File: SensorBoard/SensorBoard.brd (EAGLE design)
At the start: 160 x 100 mm, 44 parts, among them IC1 7805, J1 DCJ0202, U1 MPU-6000QFN-24, X3 MINI-USB-SCHIELD-32005-201

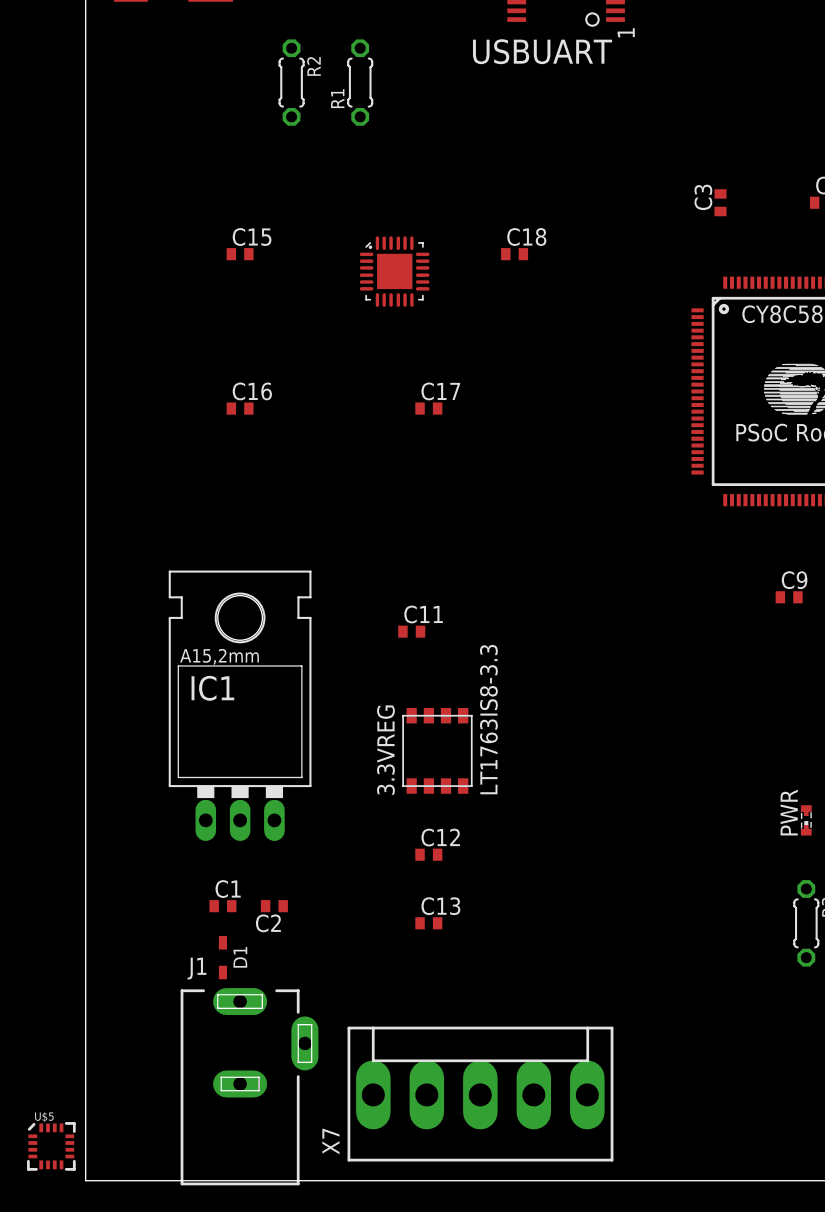
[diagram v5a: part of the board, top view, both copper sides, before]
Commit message: added magnetometer
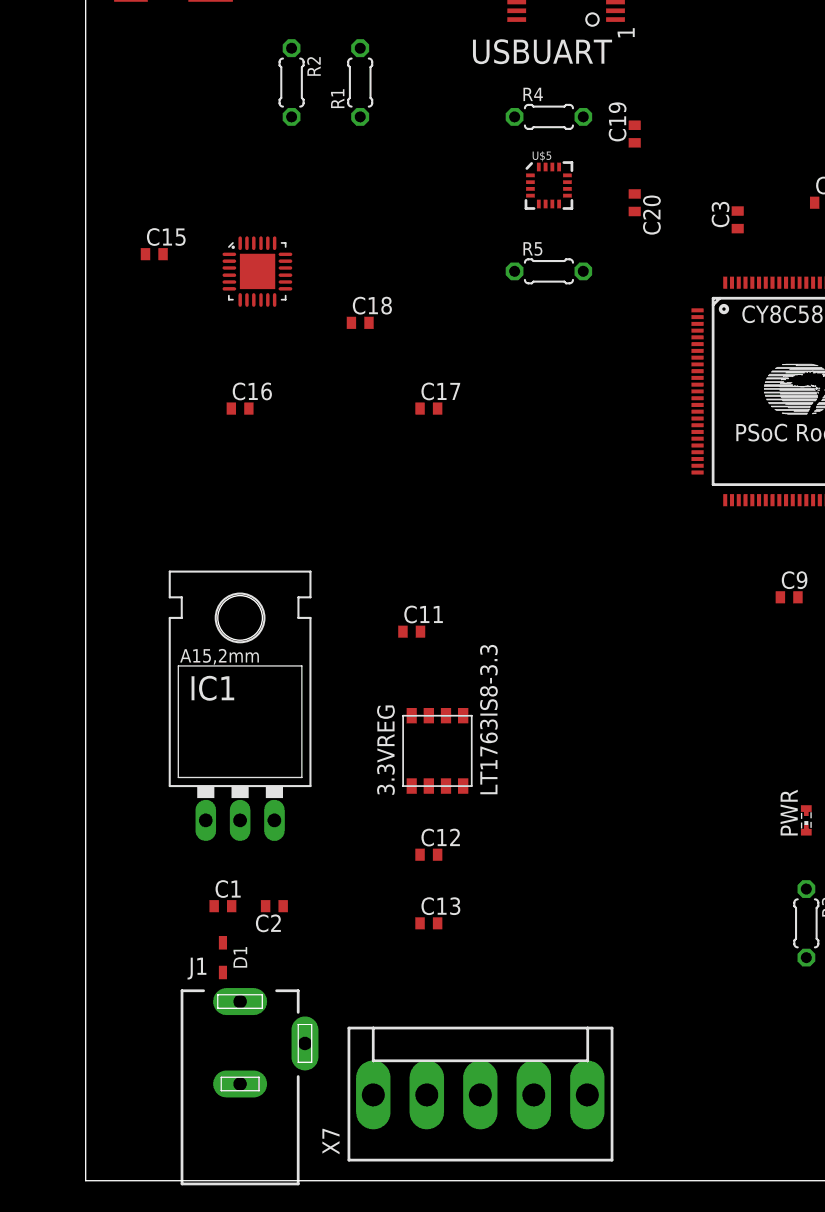
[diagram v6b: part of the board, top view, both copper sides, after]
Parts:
- added C19: .22uF, rcl:C0402
- added C20: 4.7uF, rcl:C0402
- added R4, R5: 4k, resistor:0204/5
- moved U$5 80.1 mm to (34.3, 73.7)
- moved C18 12.5 mm to (20.3, 63.5)
- moved U1 10.2 mm to (12.7, 67.3)
- moved C15 6.35 mm to (5.08, 68.6)
- moved C3 1.80 mm to (48.3, 71.1)
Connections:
- new net N$11: C19.2, U$5.12
- new net N$15: C19.1, U$5.8
- new net N$16: C20.1, U$5.10
- net +3.3V: now also R4.2, R5.2, U$5.13, U$5.2, U$5.4
- net AUXCL1: now also R4.1, U$5.1
- net AUXDA1: now also R5.1, U$5.16
- net GND: now also C20.2, U$5.11, U$5.9

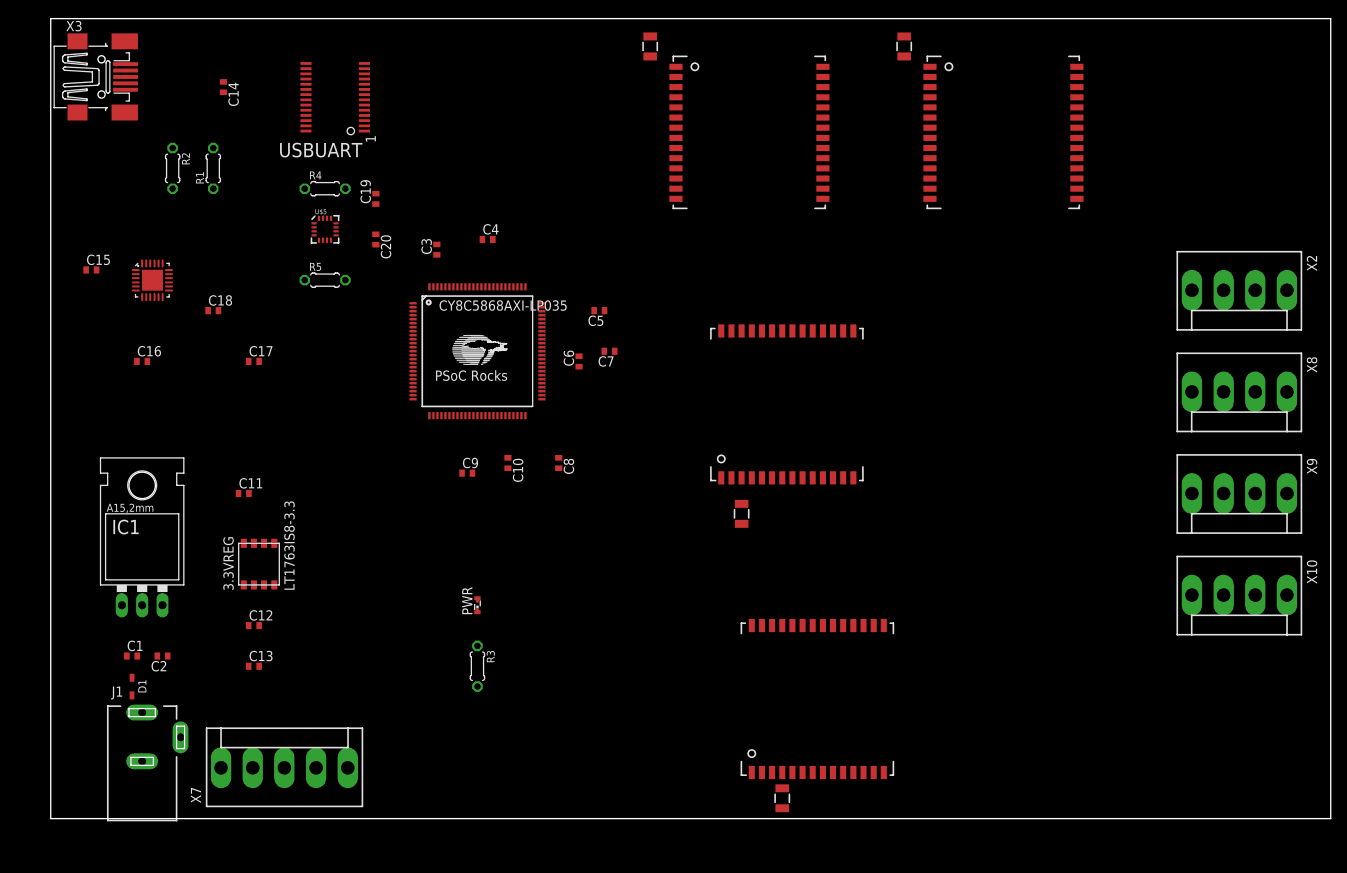
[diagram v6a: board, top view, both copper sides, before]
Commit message: added general pin io
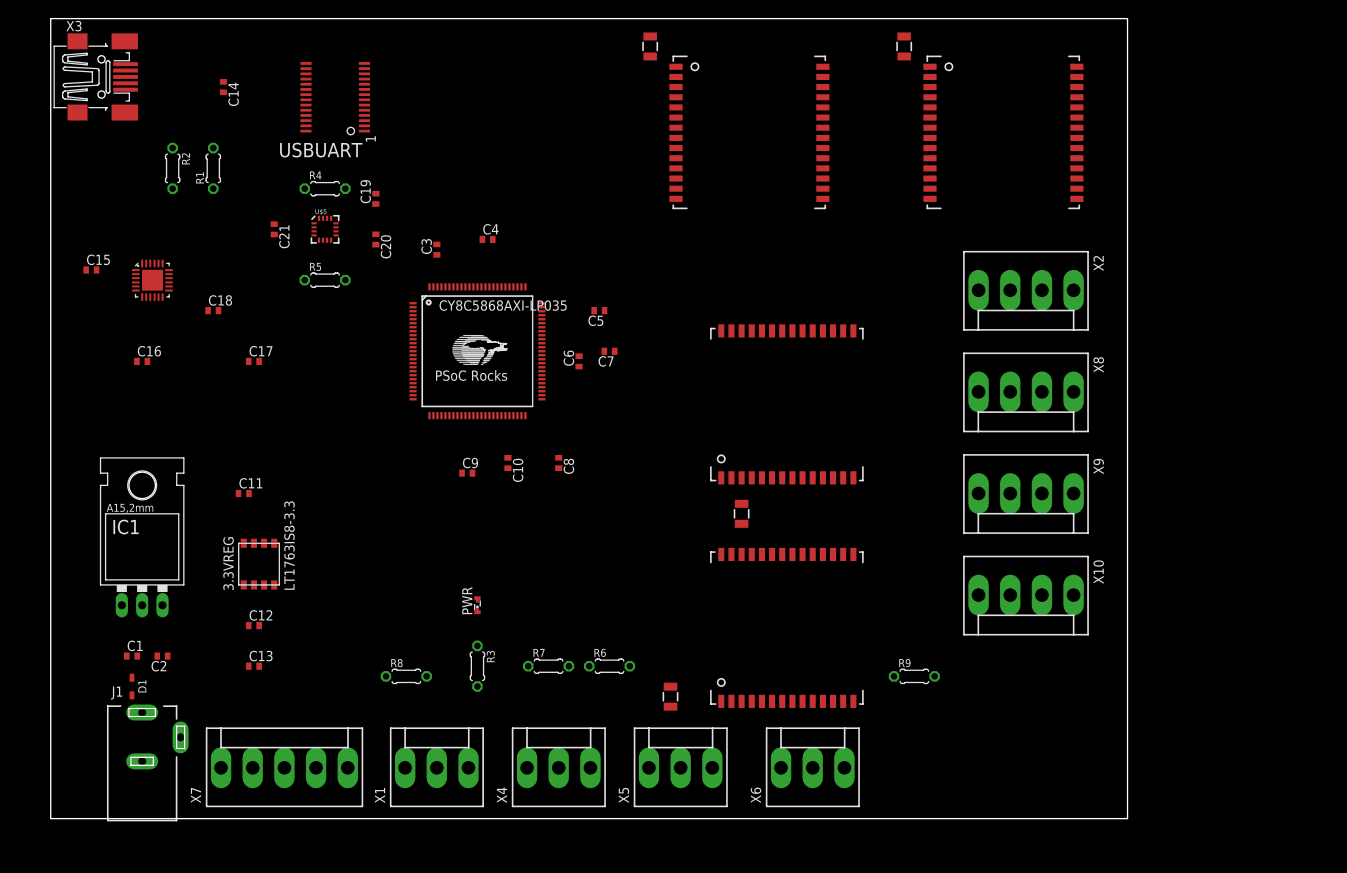
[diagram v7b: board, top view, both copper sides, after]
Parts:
- added C21: .1uF, rcl:C0402
- added R6, R7, R8, R9: 10k, resistor:0204/5
- added X1, X4, X5, X6: (no value), con-molex:KK-156-3
- moved X10 26.7 mm to (121.9, 27.9)
- moved X2 26.7 mm to (121.9, 66.0)
- moved X8 26.7 mm to (121.9, 53.3)
- moved X9 26.7 mm to (121.9, 40.6)
- moved U$4 18.9 mm to (77.5, 15.2)
- moved GPS4 9.67 mm to (83.8, 33.0)
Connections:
- removed net SCL: U1.23
- removed net SDA: U1.24
- new net GEN1: CY8C5868AXI-LP035.31, R8.2, X1.1
- new net GEN2: CY8C5868AXI-LP035.32, R7.2, X4.1
- new net GEN3: CY8C5868AXI-LP035.33, R6.2, X5.1
- new net GEN4: CY8C5868AXI-LP035.34, R9.2, X6.1
- new net SCL_ACC: CY8C5868AXI-LP035.4, U1.23
- new net SDA_ACC: CY8C5868AXI-LP035.5, U1.24
- net +3.3V: now also C21.1
- net +5V: now also X1.2, X4.2, X5.2, X6.2
- net GND: now also C21.2, R6.1, R7.1, R8.1, R9.1, X1.3, X4.3, X5.3, X6.3
- net N$8: now also C18.1
- net RX1: now also CY8C5868AXI-LP035.74
- net RX2: now also CY8C5868AXI-LP035.72
- net RX3: now also CY8C5868AXI-LP035.70
- net RX4: now also CY8C5868AXI-LP035.68
- net TX1: now also CY8C5868AXI-LP035.73
- net TX2: now also CY8C5868AXI-LP035.71
- net TX3: now also CY8C5868AXI-LP035.69
- net TX4: now also CY8C5868AXI-LP035.67
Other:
- board size 160 x 100 mm -> 134.6 x 100 mm

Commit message: added stuff to board
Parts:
- removed X10, X9: (no value), con-molex:KK-156-4
- added PI: 87758-2616, con-molex:87758-2616
- added PWR1, PWR2, PWR3, PWR4: GREEN, led:SMARTLED-TTW
- added R10, R11, R12, R13: 4k, resistor:0204/5
- added X13: 3.3out1, con-molex:KK-156-3
- added X14: 3.3out2, con-molex:KK-156-3
- added X15: uart1, con-molex:KK-156-4
- added X16: uart2, con-molex:KK-156-4
- added X17: uart3, con-molex:KK-156-4
- added X18: uart4, con-molex:KK-156-4
- X1: value (none) -> gen1
- X2: value (none) -> motordriver1; device con-molex:KK-156-4 -> con-molex:KK-156-3
- X4: value (none) -> gen2
- X5: value (none) -> gen3
- X6: value (none) -> gen4
- X8: value (none) -> motordriver2; device con-molex:KK-156-4 -> con-molex:KK-156-3
- moved X7 98.0 mm to (127.0, 12.7), turned to 90 degrees
- moved C15 94.4 mm to (95.2, 40.6), turned to 180 degrees
- moved C21 91.4 mm to (109.2, 31.8), turned to 0 degrees
- moved C16 89.2 mm to (99.1, 40.6)
- moved U1 84.7 mm to (95.2, 48.3)
- moved C20 84.7 mm to (118.1, 38.1)
- moved R4 83.5 mm to (104.1, 33.0), turned to 270 degrees
- moved C19 82.9 mm to (115.6, 41.9), turned to 180 degrees
- moved U$5 82.9 mm to (109.2, 38.1)
- moved C18 80.8 mm to (100.3, 52.1)
- moved C17 78.1 mm to (102.9, 47.0), turned to 90 degrees
- moved R5 74.8 mm to (104.1, 40.6), turned to 90 degrees
- moved U$4 72.0 mm to (132.1, 62.2), turned to 180 degrees
- moved X2 57.8 mm to (113.0, 8.89), turned to 270 degrees
- moved X8 48.9 mm to (101.6, 8.89), turned to 270 degrees
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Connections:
- new net GEN5: CY8C5868AXI-LP035.29, X13.1
- new net GEN6: CY8C5868AXI-LP035.30, X14.1
- new net GPIO10: CY8C5868AXI-LP035.82, PI.19
- new net GPIO11: CY8C5868AXI-LP035.80, PI.23
- new net GPIO14: CY8C5868AXI-LP035.1, PI.8
- new net GPIO15: CY8C5868AXI-LP035.2, PI.10
- new net GPIO17: CY8C5868AXI-LP035.85, PI.11
- new net GPIO18: CY8C5868AXI-LP035.3, PI.12
- new net GPIO2(0): CY8C5868AXI-LP035.91, PI.3
- new net GPIO22: CY8C5868AXI-LP035.83, PI.15
- new net GPIO23: CY8C5868AXI-LP035.16, PI.16
- new net GPIO24: CY8C5868AXI-LP035.17, PI.18
- new net GPIO25: CY8C5868AXI-LP035.18, PI.22
- new net GPIO27: CY8C5868AXI-LP035.84, PI.13
- new net GPIO3(1): CY8C5868AXI-LP035.90, PI.5
- new net GPIO4: CY8C5868AXI-LP035.89, PI.7
- new net GPIO7: CY8C5868AXI-LP035.52, PI.26
- new net GPIO8: CY8C5868AXI-LP035.19, PI.24
- new net GPIO9: CY8C5868AXI-LP035.81, PI.21
- new net MDTX1: CY8C5868AXI-LP035.46, X2.1
- new net MDTX2: CY8C5868AXI-LP035.45, X8.1
- new net N$17: PWR3.C@1, R11.2
- new net N$18: PWR2.C@1, R12.2
- new net N$19: PWR1.C@1, R13.2
- new net N$9: PWR4.C@1, R10.2
- new net STATUS1: CY8C5868AXI-LP035.56, PWR1.A@1
- new net STATUS2: CY8C5868AXI-LP035.55, PWR2.A@1
- new net STATUS3: CY8C5868AXI-LP035.54, PWR3.A@1
- new net STATUS4: CY8C5868AXI-LP035.53, PWR4.A@1
- net +3.3V: now also PI.1, PI.17, X13.2, X14.2
- net +5V: now also PI.2, PI.4, X15.3, X16.3, X17.3, X18.3; no longer X10.2, X9.2
- net GND: now also PI.14, PI.20, PI.25, PI.6, PI.9, R10.1, R11.1, R12.1, R13.1, X13.3, X14.3, X15.4, X16.4, X17.4, X18.4, X2.3, X8.3; no longer X10.1, X2.1, X8.1, X9.1
- net RX1: now also X15.1; no longer X2.4
- net RX2: now also X16.1; no longer X8.4
- net RX3: now also X17.1; no longer X9.4
- net RX4: now also X18.1; no longer X10.4
- net TX1: now also X15.2; no longer X2.3
- net TX2: now also X16.2; no longer X8.3
- net TX3: now also X17.2; no longer X9.3
- net TX4: now also X18.2; no longer X10.3
